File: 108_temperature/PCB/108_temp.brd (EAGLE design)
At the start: 25.4 x 33 mm, 4 parts, among them U1 SENSOR-LM60-TO92

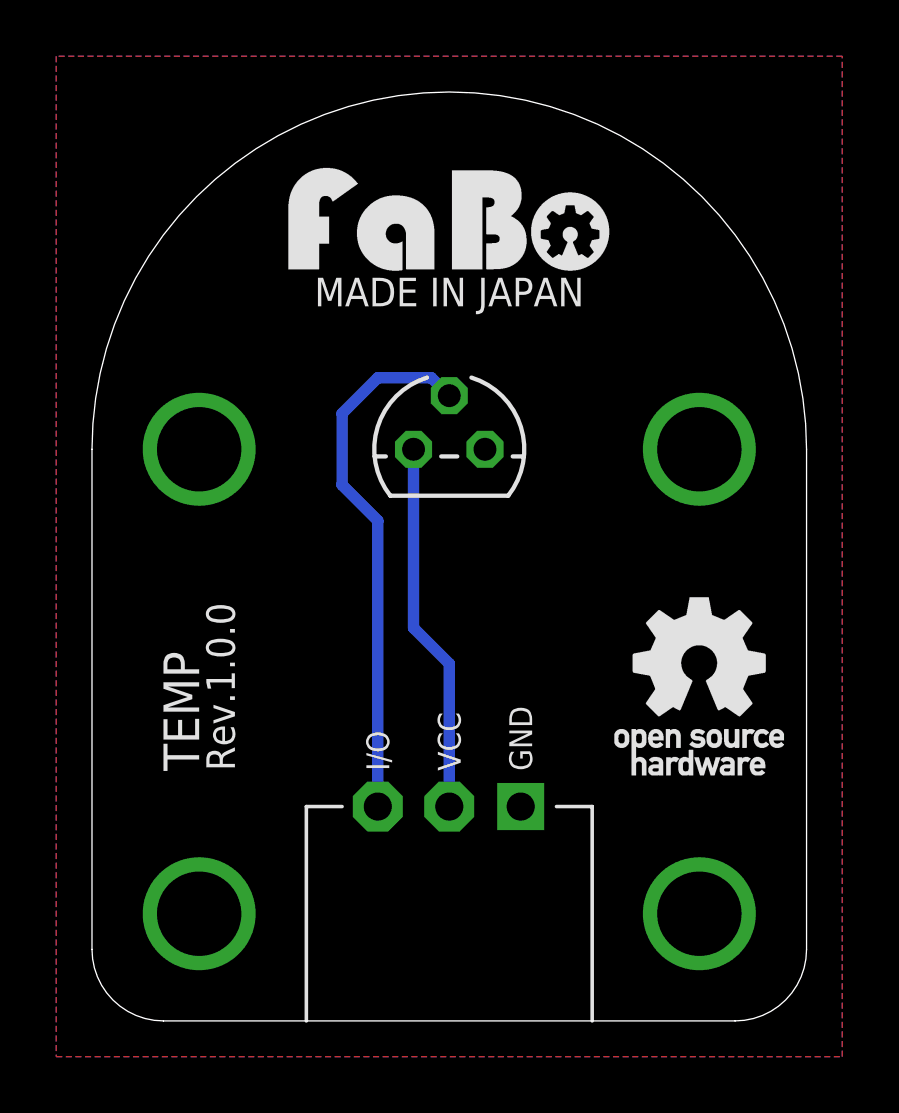
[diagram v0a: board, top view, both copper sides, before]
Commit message: add product number
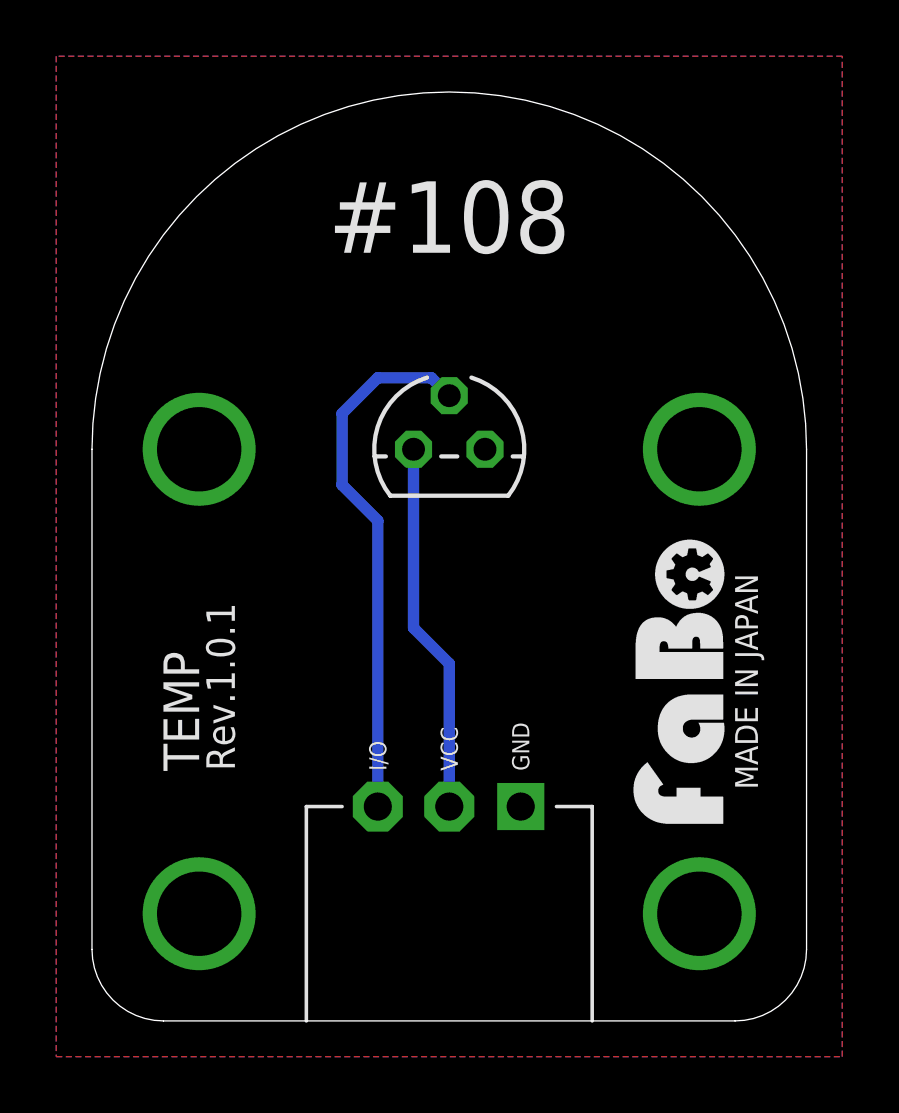
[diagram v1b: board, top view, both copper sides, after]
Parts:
- U$2: device FaBo-etc:LOGO_OSHW_T_M -> FaBo-etc:LOGO_OSHW_T_MS_BOTTOM
- U$3: device FaBo-etc:LOGO_FABO_M -> FaBo-etc:LOGO_FABO_MS
- moved U$3 17.8 mm to (22.9, 12.1), turned to 90 degrees
- moved U$2 12.6 mm to (12.7, 3.81)
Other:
- board text added: "#108"
- board text added: "Rev.1.0.1"
- board text removed: "Rev.1.0.0"
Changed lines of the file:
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@@
 <plain>
 <text x="3.81" y="8.89" size="1.27" layer="21" font="vector" ratio="12" rot="R90">TEMP</text>
-<text x="5.08" y="8.89" size="1.016" layer="21" font="vector" ratio="12" rot="R90">Rev.1.0.0</text>
-<text x="12.7" y="25.4" size="1.016" layer="21" font="vector" ratio="12" align="bottom-center">MADE IN JAPAN</text>
+<text x="5.08" y="8.89" size="1.016" layer="21" font="vector" ratio="12" rot="R90">Rev.1.0.1</text>
+<text x="22.86" y="12.065" size="0.8128" layer="21" font="vector" ratio="12" rot="R270" align="bottom-center">MADE IN JAPAN</text>
+<text x="12.7" y="27.305" size="2.54" layer="21" font="vector" ratio="12" align="bottom-center">#108</text>
 </plain>
 <attributes>
@@
 <element name="U1" library="Gclue" package="SENSOR-LM60-TO-92" value="SENSOR-LM60-TO92" x="12.7" y="20.32" smashed="yes"/>
 <element name="J1" library="FaBo-Template" package="FABO_BRICK_3PIN" value="" x="12.7" y="16.51"/>
-<element name="U$2" library="FaBo-etc" package="LOGO_OSHW_T_M" value="" x="21.59" y="12.7"/>
-<element name="U$3" library="FaBo-etc" package="LOGO_FABO_M" value="" x="12.7" y="26.67"/>
+<element name="U$3" library="FaBo-etc" package="LOGO_FABO_MS" value="" x="22.86" y="12.065" rot="R90"/>
+<element name="U$2" library="FaBo-etc" package="LOGO_OSHW_T_MS_BOTTOM" value="" x="12.7" y="3.81"/>
 </elements>
 <signals>
